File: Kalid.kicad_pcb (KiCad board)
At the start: 4 copper layers, 90 x 40 mm, 153 parts, among them J1 USB_A, J3 USB_A, J31 DC Connector, J4 USB_A, J5 USB_A, J6 Conn_01x04, J7 USB_C_Receptacle_USB2.0_16P, U1 TPS62933, U2 TPS62933, U3 GL3523-OTY30, U4 USB-PD, U5 LPW5209AB5F, U6 LPW5209AB5F, U7 LPW5209AB5F, U8 LPW5209AB5F, U9 MX25L1006EMI-10G, Y1 Crystal 25MHz 2016

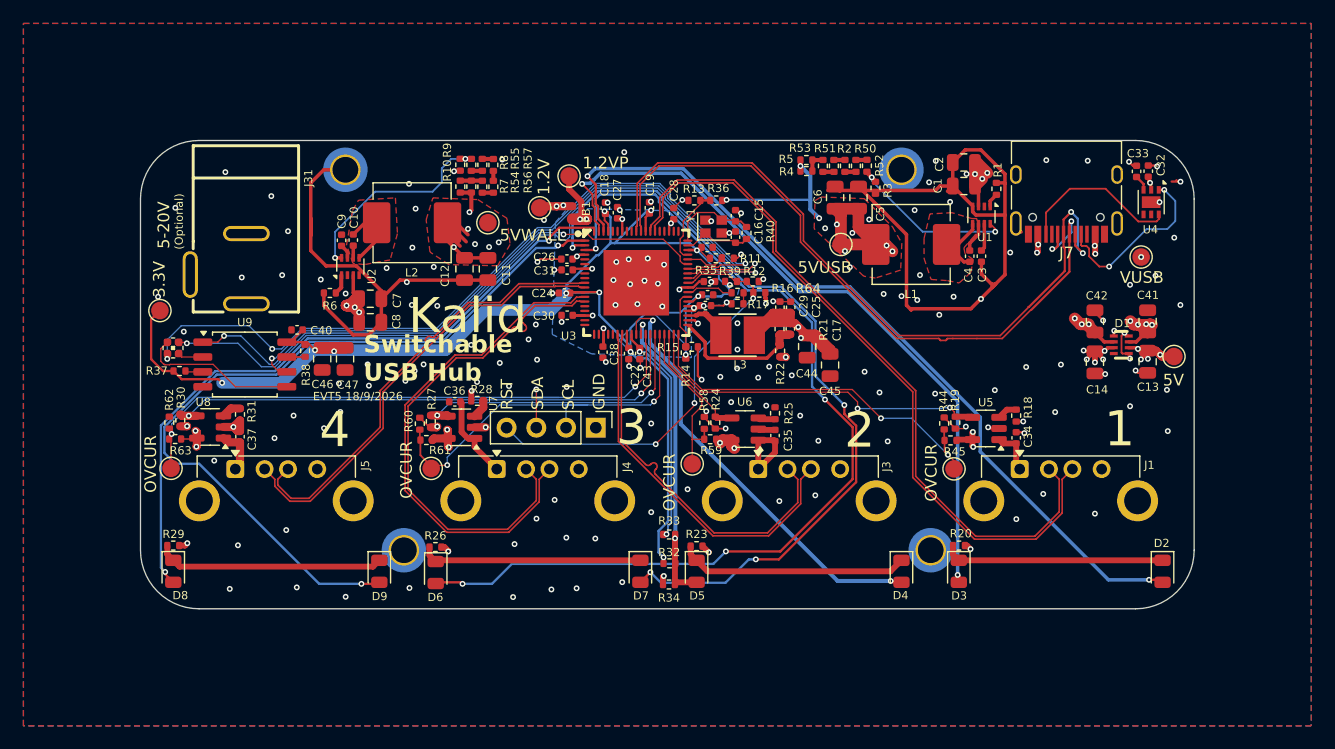
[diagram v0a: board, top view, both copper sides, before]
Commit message: add second power circuit
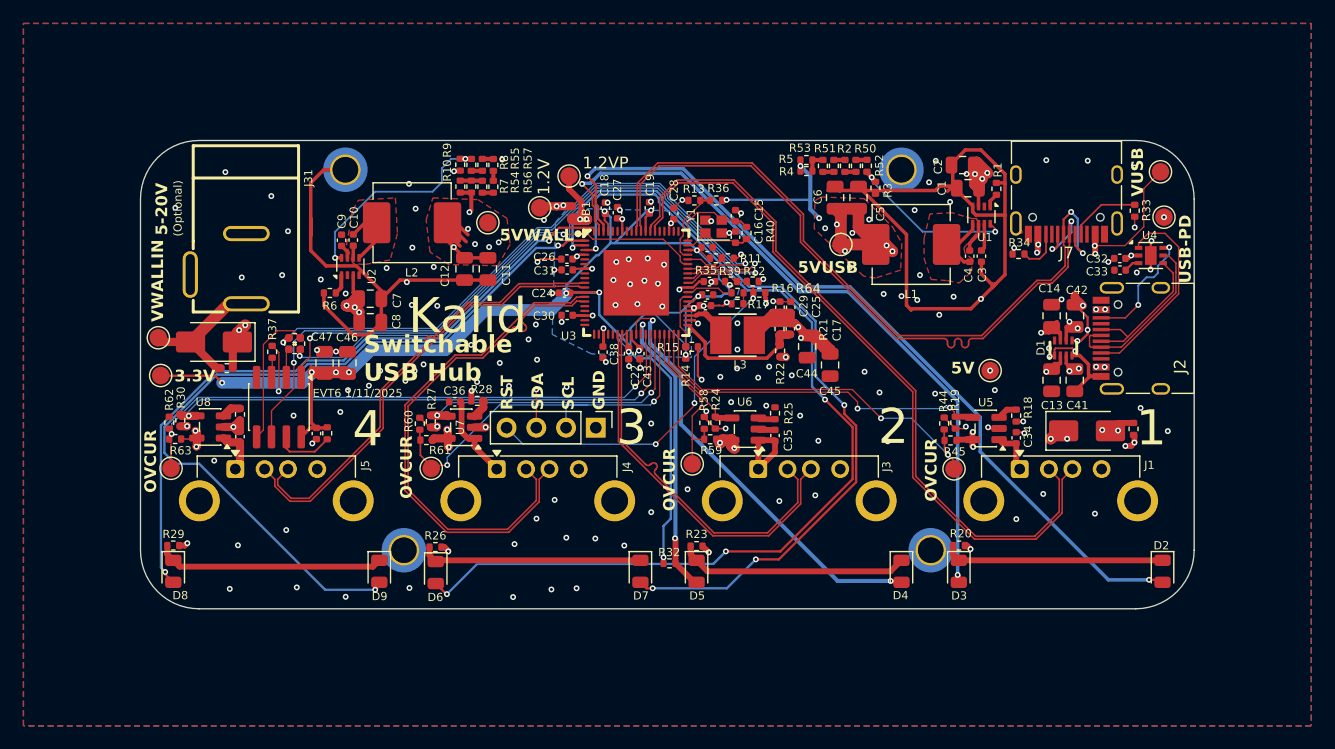
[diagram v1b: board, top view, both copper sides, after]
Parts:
- added D10: SS34, Diode_SMD:D_SMA, F.Cu at (106.3, 82.2)
- added D11: SS34, Diode_SMD:D_SMA, F.Cu at (180.8, 89.8)
- added J2: USB_C_Receptacle_USB2.0_16P, Kalid:USB_C_Receptacle_HRO_TYPE-C-31-M-12, F.Cu at (186.1, 81.9)
- added R47: R 0 ohm 0402, Resistor_SMD:R_0402_1005Metric, F.Cu at (107.4, 84.5)
- added R48: R 0 ohm 0402, Resistor_SMD:R_0402_1005Metric, F.Cu at (184.8, 89.6)
- added TP12: TestPoint, TestPoint:TestPoint_Pad_D1.5mm, F.Cu at (101.5, 81.8)
- added TP13: TestPoint, TestPoint:TestPoint_Pad_D1.5mm, F.Cu at (187.4, 71.5)
- R32: value R 10k 0402 -> R 1k 0402
- R33, R34: value R 10k 0402 -> R 5.1k 0402
- U9: footprint Package_SO:SOIC-8_5.3x5.3mm_P1.27mm -> Package_SO:SOP-8_3.76x4.96mm_P1.27mm
- moved R33 48.4 mm to (184.9, 71.0), turned to 90 degrees
- moved R34 41.1 mm to (175.0, 74.7)
- moved TP2 15.7 mm to (172.6, 84.7)
- moved R46 10.9 mm to (113.2, 81.9), turned to 180 degrees
- moved R41 10.9 mm to (113.6, 82.3), turned to -90 degrees
- moved R42 9.96 mm to (112.7, 82.3), turned to 90 degrees
- moved R43 9.92 mm to (113.2, 82.8), turned to 0 degrees
- moved C40 9.01 mm to (115.0, 90.0), turned to -90 degrees
- moved C33 8.55 mm to (183.7, 76.1), turned to 180 degrees
- moved C13 8.35 mm to (177.8, 85.5)
- moved R37 8.09 mm to (111.2, 83.0), turned to 90 degrees
- moved C41 8.00 mm to (179.8, 85.5), turned to -90 degrees
- moved C32 7.84 mm to (183.7, 75.1), turned to 180 degrees
- moved TP7 7.47 mm to (187.1, 67.7)
- moved R38 7.30 mm to (116.0, 90.0)
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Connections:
- C32 pad 1: +VUSBIN -> +VUSBEXTRA
- C41 pad 1: +V5VWALL -> +V5VUSB
- C42 pad 1: +V5VUSB -> +V5VWALL
- C7 pad 1: +VWALLIN -> +VEXTRA
- C8 pad 1: +VWALLIN -> +VEXTRA
- D1 pad 3: +V5VWALL -> +V5VUSB
- D1 pad 6: +V5VUSB -> +V5VWALL
- R33 pad 1: +1.2V -> GND
- R33 pad 2: Net-(D5-A) -> /Hierarchy/USB/CC1
- R34 pad 1: +V5V -> GND
- R34 pad 2: Net-(D5-A) -> /Hierarchy/USB/CC2
- U2 pad 3: +VWALLIN -> +VEXTRA
- U4 pad 1: /Hierarchy/USB/CC1 -> /Hierarchy/Power/EXTRA_CC1
- U4 pad 2: +VUSBIN -> +VUSBEXTRA
- U4 pad 4: unconnected-(U4-D+-Pad4) -> Net-(U4-D+)
- U4 pad 5: unconnected-(U4-D--Pad5) -> Net-(U4-D-)
- U4 pad 6: /Hierarchy/USB/CC2 -> /Hierarchy/Power/EXTRA_CC2
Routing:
- net +VEXTRA: track 0.00 -> 141.4 mm, vias 0 -> 9
- net +VUSBEXTRA: track 0.00 -> 30.0 mm, vias 0 -> 8
- net +1.2V: track 85.2 -> 67.0 mm, vias 8 -> 7
- net /Hierarchy/Power/EXTRA_CC1: track 0.00 -> 17.4 mm
- net Net-(U4-D-): track 0.00 -> 15.1 mm
- net Net-(U4-D+): track 0.00 -> 13.2 mm
- net Net-(U3B-P_SPI_DI): track 66.7 -> 54.0 mm, vias 3 -> 2
- net GND: track 141.8 -> 153.5 mm, vias 162 -> 155
- net Net-(U3B-P_SPI_DO): track 67.1 -> 56.2 mm
- net /Hierarchy/Power/EXTRA_CC2: track 0.00 -> 10.6 mm, vias 0 -> 2
- net +V5VWALL: track 88.2 -> 77.9 mm, vias 10 -> 8
- net /Hierarchy/USB/CC2: track 14.0 -> 3.78 mm
- net /Hierarchy/USB/CC1: track 15.3 -> 6.08 mm, vias 2 -> 0
- net /Hierarchy/USB/SPI_CS: track 48.5 -> 40.8 mm
- net /Hierarchy/USB/SPI_CLK: track 58.2 -> 63.3 mm
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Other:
- board text added: "EVT6 1/11/2025"
- board text added: "USB-PD"
- board text added: "VWALLIN"
- board text removed: "EVT5 18/9/2026"

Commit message: evt5: Release
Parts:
- R20, R23, R26, R29: value R 510 0402 -> R 1k 0402
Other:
- board text added: "Data"
- board text added: "Power"
